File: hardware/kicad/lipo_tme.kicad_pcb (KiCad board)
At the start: 2 copper layers, 70 x 50 mm, 62 parts

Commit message: hardware: UART debug header on all boards, I2C header and rail test pads on carrier, SDA/SCL pads on pack
Header is 1x3 2.54 mm (GND, MCU TX, MCU RX), hand-soldered, kept out of the BOM.
Carrier uses Heltec UART0 (GPIO43/44), STM32 boards USART1 (PA9/PA10).

Co-Authored-By: Claude Sonnet 5.5 <noreply@anthropic.com>
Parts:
- added J_UART1: UART, Connector_PinHeader_2.54mm:PinHeader_1x03_P2.54mm_Vertical, F.Cu at (29.3, 40.5)
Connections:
- U_MCU pad 19: unconnected-(U_MCU-PA9-Pad19) -> UART_TX
- U_MCU pad 20: unconnected-(U_MCU-PA10-Pad20) -> UART_RX
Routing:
- net SDA_EXT: track 66.1 -> 55.3 mm, vias 1 -> 3
- net VBAT_SW: track 46.3 -> 57.1 mm, vias 1 -> 2
- net REV_G: track 28.5 -> 18.1 mm, vias 3 -> 2
- net TAP2_ADC: track 55.2 -> 45.5 mm
- net UART_TX: track 0.00 -> 7.75 mm, vias 0 -> 1
- net KILL_DRV: track 52.2 -> 44.7 mm
- net +5V: track 50.6 -> 58.0 mm
- net SCL_EXT: track 60.7 -> 53.4 mm
- net BOOT0: track 27.4 -> 22.6 mm
- net UART_RX: track 0.00 -> 3.61 mm
- net GND: track 292.6 -> 289.4 mm
- net KILL_G: track 17.3 -> 14.2 mm
- net SWCLK: track 16.6 -> 19.8 mm
- net VIN: track 117.4 -> 114.2 mm
- net FB_A: track 12.2 -> 9.24 mm
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
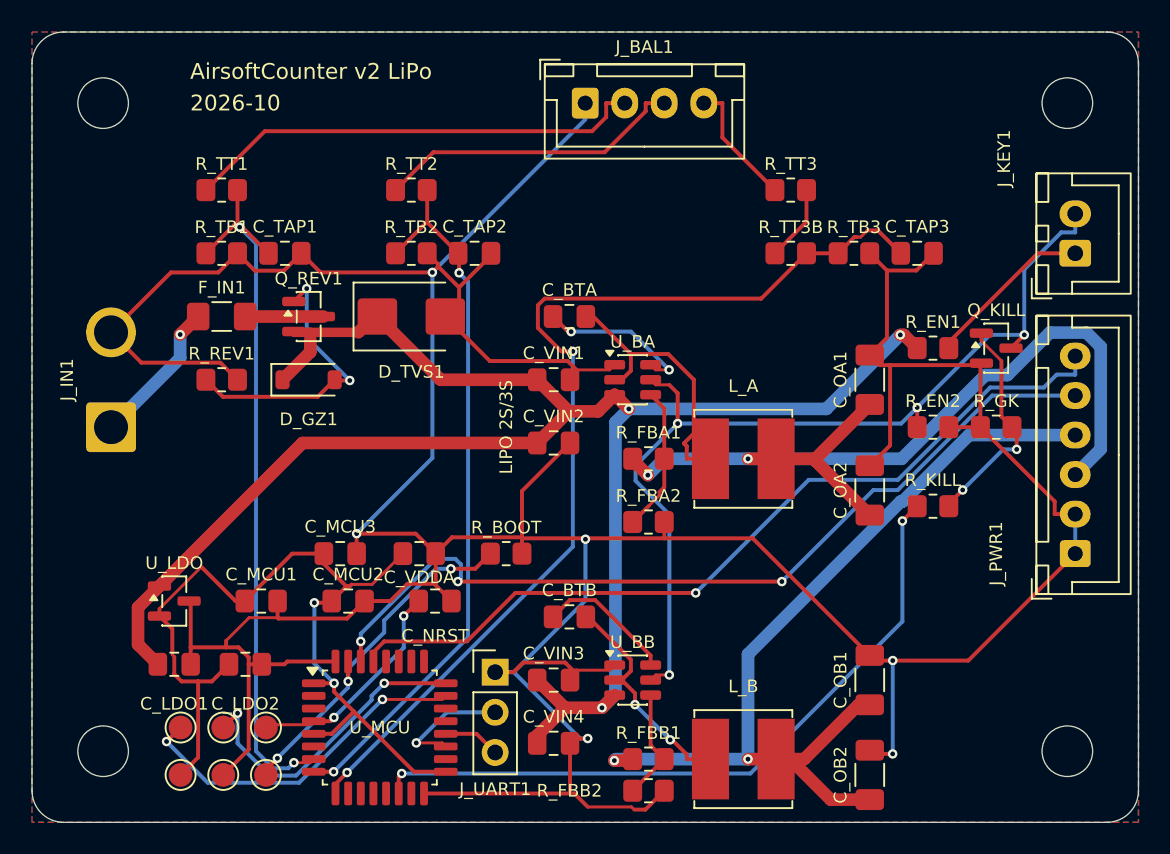
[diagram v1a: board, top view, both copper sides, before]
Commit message: hardware: KiCad 10 pipeline fixes, +5V reservoir caps, NS4168 1uF, pack UART header off the holders
KiCad 9 -> 10.0.7 broke the generators even on HEAD:
- gen_sch: libraries moved (hide yes) from effects to the property; read both,
  write it back into effects (KiCad 9 format), so hidden fields stop showing
  on every sheet and stop blocking the schematic router. Add the title block.
- gen_pcb: SetDoNotAllowCopperPour -> SetDoNotAllowZoneFills; copy the symbol's
  Datasheet/Description/Sim fields onto footprints (schematic parity now fails
  DRC); refuse THT pads under bottom-side parts (PTH_UNDER_OK allowlist).
- route.py: Power class routed at +40 um (Freerouting's octagons undercut 0.8 mm
  round ends, KiCad 10 exports no clearance margin), falling back to no margin
  if that leaves a connection unrouted; strip dangling stubs after SES import.
- pack: USB-C shield pin S1 -> SH; pack_tme: VSSOP-10 -> MSOP-10 footprint.

Design changes from the Konnect MCP review and datasheet check:
- carrier: C_5V1 10 uF + C_5V2 100 nF on +5V at J_PWR1 (no local cap before);
  C_AMP2 100 nF -> 1 uF per NS4168 datasheet (100 uF || 1 uF). carrier_tme
  places the new caps clear of its DAC.
- pack/pack_tme: J_UART1 sat under BT4 (bottom-side 18650 holder), caught by
  KiCad 10's pth_inside_courtyard; moved to the right strip, label in pin order.
  The NTC beads stay in the holder window (check ignored, gen_pcb enforces it).
- Docs: ORDERING counts, NS4168/TCA9534/BSS138/1N4148W datasheet check,
  TCA9534 P6/P7 firmware note.

All six boards: ERC 0, DRC 0 (0 unconnected, 0 parity), gerbers ok.

Co-Authored-By: Claude Opus 5.5 <noreply@anthropic.com>
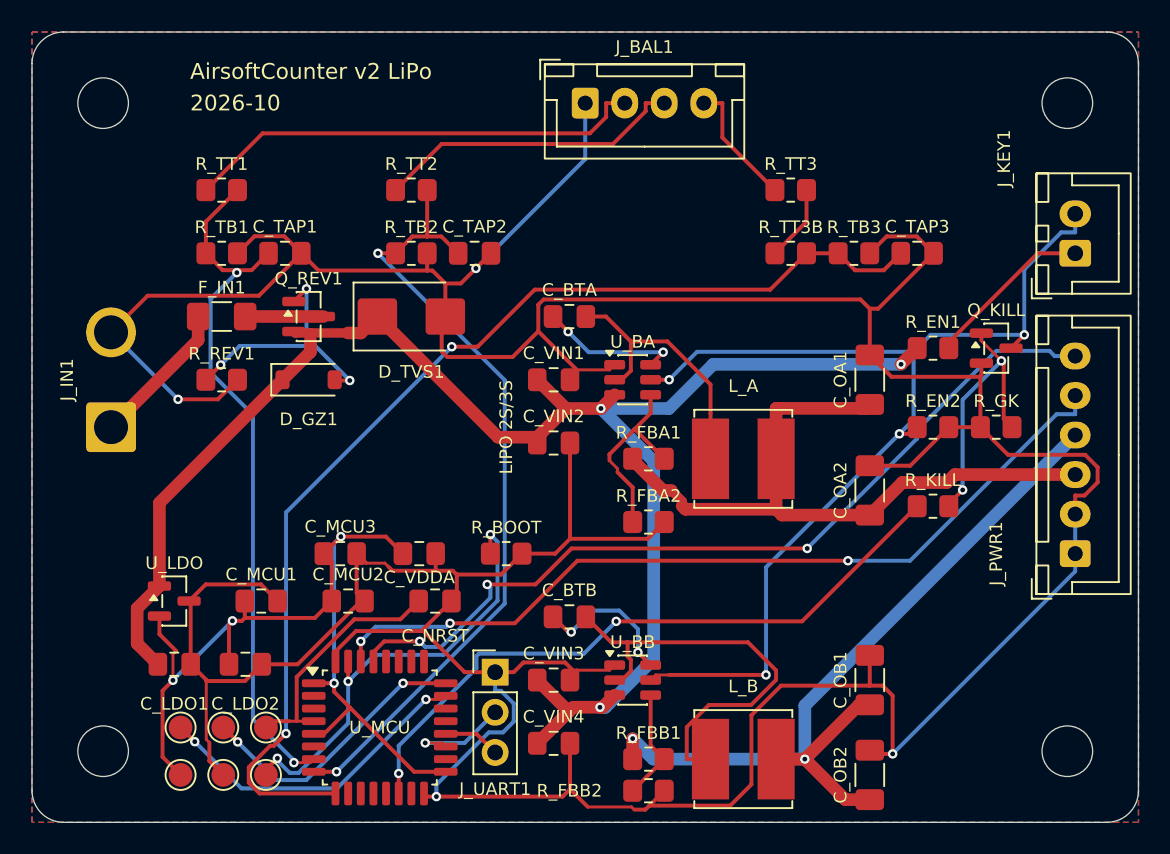
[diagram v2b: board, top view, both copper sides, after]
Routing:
- net GND: track 289.4 -> 310.7 mm, vias 6 -> 4
- net VBAT_SW: track 57.1 -> 43.2 mm, vias 2 -> 0
- net SW_B: track 14.2 -> 27.6 mm, vias 2 -> 0
- net BUCK_EN: track 59.4 -> 68.6 mm
- net VIN: track 114.2 -> 106.5 mm
- net TAP3_ADC: track 64.0 -> 70.6 mm
- net BOOT0: track 22.6 -> 28.6 mm
- net TAP2_ADC: track 45.5 -> 50.9 mm
- net +5V: track 58.0 -> 52.8 mm
- net KILL_G: track 14.2 -> 17.3 mm
- net FB_A: track 9.24 -> 12.4 mm
- net KILL_DRV: track 44.7 -> 42.5 mm
- net +3V3: track 57.9 -> 59.9 mm, vias 2 -> 4
- net SWCLK: track 19.8 -> 18.0 mm
- net SDA_EXT: track 55.3 -> 53.6 mm
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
